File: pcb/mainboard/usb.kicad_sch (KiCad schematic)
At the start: 9 parts, among them J801 USB_B_Mini, U800 USBLC6-2P6

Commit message: Mainboard schematics WIP
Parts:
- gave numbers to parts that had none: 4
- renumbered C837 to C801, L800 to L801, U800 to U802
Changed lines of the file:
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@@
   (symbol (lib_id "Device:C") (at 175.26 92.71 0) (mirror y) (unit 1)
     (in_bom yes) (on_board yes)
-    (property "Reference" "C837" (id 0) (at 172.339 91.542 0)
+    (property "Reference" "C801" (id 0) (at 172.339 91.542 0)
       (effects (font (size 1.27 1.27)) (justify left))
     )
@@
   (symbol (lib_id "power:GND") (at 203.2 109.22 0) (mirror y) (unit 1)
     (in_bom yes) (on_board yes)
-    (property "Reference" "#PWR0291" (id 0) (at 203.2 115.57 0)
+    (property "Reference" "#PWR0804" (id 0) (at 203.2 115.57 0)
       (effects (font (size 1.27 1.27)) hide)
     )
@@
   (symbol (lib_id "power:GND") (at 226.06 129.54 0) (mirror y) (unit 1)
     (in_bom yes) (on_board yes)
-    (property "Reference" "#PWR0292" (id 0) (at 226.06 135.89 0)
+    (property "Reference" "#PWR0806" (id 0) (at 226.06 135.89 0)
       (effects (font (size 1.27 1.27)) hide)
     )
@@
   (symbol (lib_id "power:VBUS") (at 175.26 86.36 0) (mirror y) (unit 1)
     (in_bom yes) (on_board yes)
-    (property "Reference" "#PWR0295" (id 0) (at 175.26 90.17 0)
+    (property "Reference" "#PWR0802" (id 0) (at 175.26 90.17 0)
       (effects (font (size 1.27 1.27)) hide)
     )
@@
   (symbol (lib_id "power:GND") (at 175.26 96.52 0) (mirror y) (unit 1)
     (in_bom yes) (on_board yes)
-    (property "Reference" "#PWR0155" (id 0) (at 175.26 102.87 0)
+    (property "Reference" "#PWR0803" (id 0) (at 175.26 102.87 0)
       (effects (font (size 1.27 1.27)) hide)
     )
@@
   (symbol (lib_id "Power_Protection:USBLC6-2P6") (at 203.2 99.06 0) (unit 1)
     (in_bom yes) (on_board yes)
-    (property "Reference" "U800" (id 0) (at 203.2 83.82 0))
+    (property "Reference" "U802" (id 0) (at 203.2 83.82 0))
     (property "Value" "USBLC6-2P6" (id 1) (at 203.2 86.36 0))
     (property "Footprint" "Package_TO_SOT_SMD:SOT-666" (id 2) (at 203.2 111.76 0)
@@
   (symbol (lib_id "power:GND") (at 139.7 111.76 0) (mirror y) (unit 1)
     (in_bom yes) (on_board yes)
-    (property "Reference" "#PWR?" (id 0) (at 139.7 118.11 0)
+    (property "Reference" "#PWR0801" (id 0) (at 139.7 118.11 0)
       (effects (font (size 1.27 1.27)) hide)
     )
@@
   (symbol (lib_id "Device:R") (at 223.52 100.33 0) (unit 1)
     (in_bom yes) (on_board yes)
-    (property "Reference" "R?" (id 0) (at 226.06 99.06 0)
+    (property "Reference" "R803" (id 0) (at 226.06 99.06 0)
       (effects (font (size 1.27 1.27)) (justify left))
     )
@@
   (symbol (lib_id "Device:R") (at 223.52 92.71 0) (unit 1)
     (in_bom yes) (on_board yes)
-    (property "Reference" "R?" (id 0) (at 226.06 91.44 0)
+    (property "Reference" "R802" (id 0) (at 226.06 91.44 0)
       (effects (font (size 1.27 1.27)) (justify left))
     )
@@
   (symbol (lib_id "symbols:MIMX8MN6DVTJZAA") (at 111.76 83.82 0) (unit 2)
     (in_bom yes) (on_board yes) (fields_autoplaced)
-    (property "Reference" "U?" (id 0) (at 111.76 83.82 0))
+    (property "Reference" "U201" (id 0) (at 111.76 83.82 0))
     (property "Value" "MIMX8MN6DVTJZAA" (id 1) (at 111.76 86.36 0))
     (property "Footprint" "footprint:BGA-486_27x27_14.0x14.0mm" (id 2) (at 111.76 83.82 0)
@@
   (symbol (lib_id "Device:R") (at 133.35 109.22 90) (unit 1)
     (in_bom yes) (on_board yes)
-    (property "Reference" "R?" (id 0) (at 129.54 107.95 90)
+    (property "Reference" "R801" (id 0) (at 129.54 107.95 90)
       (effects (font (size 1.27 1.27)) (justify left))
     )
@@
   (symbol (lib_id "Device:L_Coupled_Small_1423") (at 175.26 120.65 0) (unit 1)
     (in_bom yes) (on_board yes)
-    (property "Reference" "L800" (id 0) (at 175.26 114.3 0))
+    (property "Reference" "L801" (id 0) (at 175.26 114.3 0))
     (property "Value" "EXC14CE900U" (id 1) (at 175.26 116.84 0))
     (property "Footprint" "footprint:L_CommonModeChoke_Panasonic_EXC14CE" (id 2) (at 175.26 120.65 0)
@@
   (symbol (lib_id "power:GND") (at 223.52 104.14 0) (mirror y) (unit 1)
     (in_bom yes) (on_board yes)
-    (property "Reference" "#PWR?" (id 0) (at 223.52 110.49 0)
-      (effects (font (size 1.27 1.27)) hide)
-    )
+    (property "Reference" "#PWR0805" (id 0) (at 223.52 110.49 0)
+      (effects (font (size 1.27 1.27)) hide)
+    )

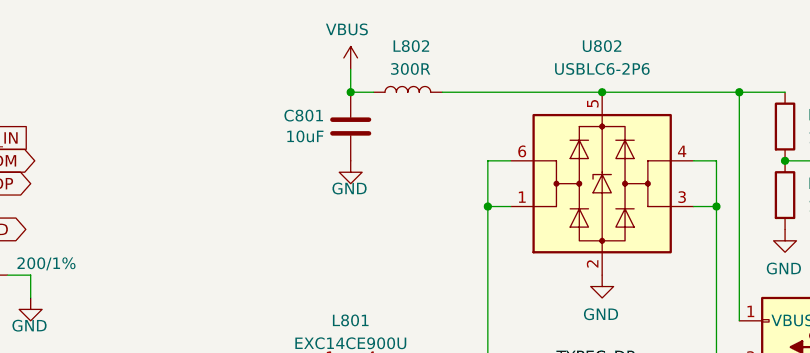
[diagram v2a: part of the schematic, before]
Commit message: Draft motherboard schematics for r0.0 layout
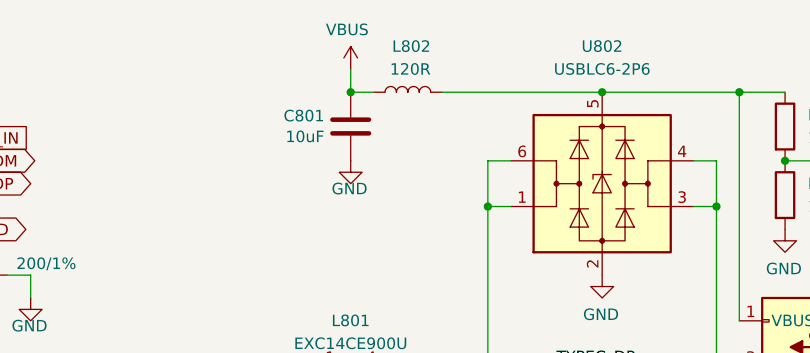
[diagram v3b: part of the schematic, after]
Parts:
- L802: value 300R -> 120R
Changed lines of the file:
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@@
       (effects (font (size 1.27 1.27)) (justify left))
     )
-    (property "Value" "300R" (id 1) (at 184.15 86.36 90)
+    (property "Value" "120R" (id 1) (at 184.15 86.36 90)
       (effects (font (size 1.27 1.27)) (justify left))
     )

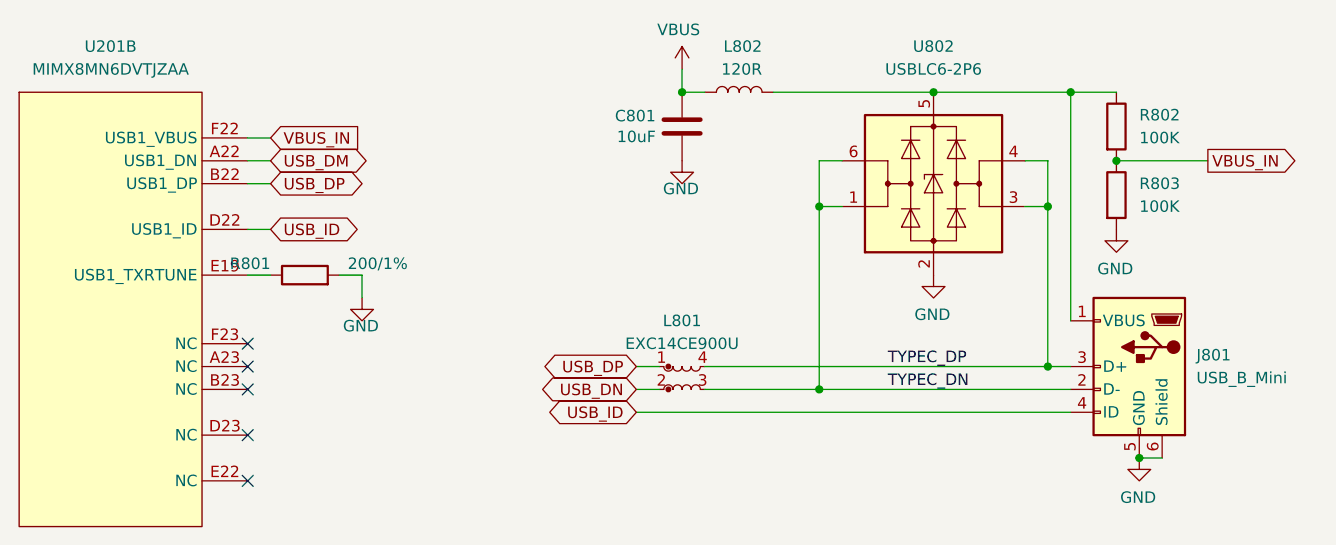
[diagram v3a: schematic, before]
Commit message: Motherboard PCB component initial placement, schematics fixes
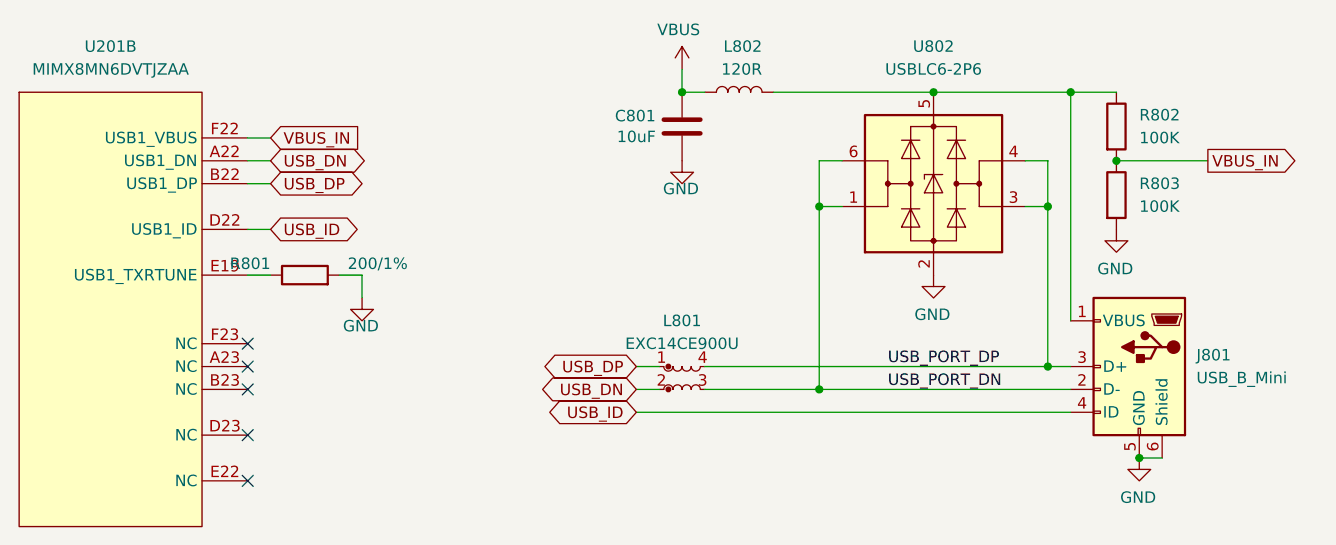
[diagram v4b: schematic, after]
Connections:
- net USB_DM is gone; now on net USB_DN: U201.A22 (USB1_DN)
- net TYPEC_DN renamed USB_PORT_DN
- net TYPEC_DP renamed USB_PORT_DP
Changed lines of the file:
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@@
     (stroke (width 0) (type default) (color 0 0 0 0))
   )
-  (label "TYPEC_DN" (at 198.12 121.92 0)
+  (label "USB_PORT_DN" (at 198.12 121.92 0)
     (effects (font (size 1.27 1.27)) (justify left bottom))
   )
-  (label "TYPEC_DP" (at 198.12 119.38 0)
+  (label "USB_PORT_DP" (at 198.12 119.38 0)
     (effects (font (size 1.27 1.27)) (justify left bottom))
   )
@@
     )
   )
-  (global_label "USB_DM" (shape bidirectional) (at 129.54 96.52 0)
+  (global_label "USB_DN" (shape bidirectional) (at 129.54 96.52 0)
     (effects (font (size 1.27 1.27)) (justify left))
     (property "Intersheet References" "${INTERSHEET_REFS}" (id 0) (at 140.9761 96.5994 0)

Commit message: Routing mainboard in progress, schematics fixes
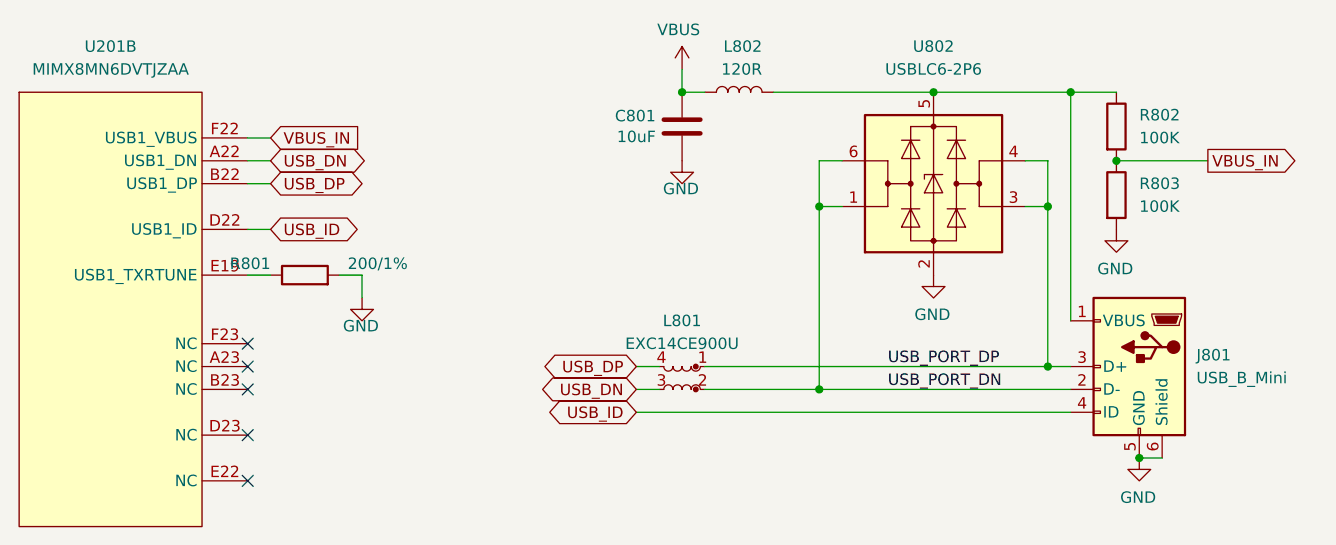
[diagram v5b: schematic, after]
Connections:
- net USB_DN: now also L801.3; no longer L801.2
- net USB_DP: now also L801.4; no longer L801.1
- net USB_PORT_DN: now also L801.2; no longer L801.3
- net USB_PORT_DP: now also L801.1; no longer L801.4
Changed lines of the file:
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@@
     (pin "2")
   )
-  (symbol (lib_id "Device:L_Coupled_Small_1423") (at 175.26 120.65 0) (unit 1)
+  (symbol (lib_id "Device:L_Coupled_Small_1423") (at 175.26 120.65 0) (mirror y) (unit 1)
     (in_bom yes) (on_board yes)
     (property "Reference" "L801" (id 0) (at 175.26 114.3 0))
